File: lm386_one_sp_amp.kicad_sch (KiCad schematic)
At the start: 20 parts, among them J1 AudioJack3, J2 AudioJack2, SW1 SW_SPST, U1 LM386

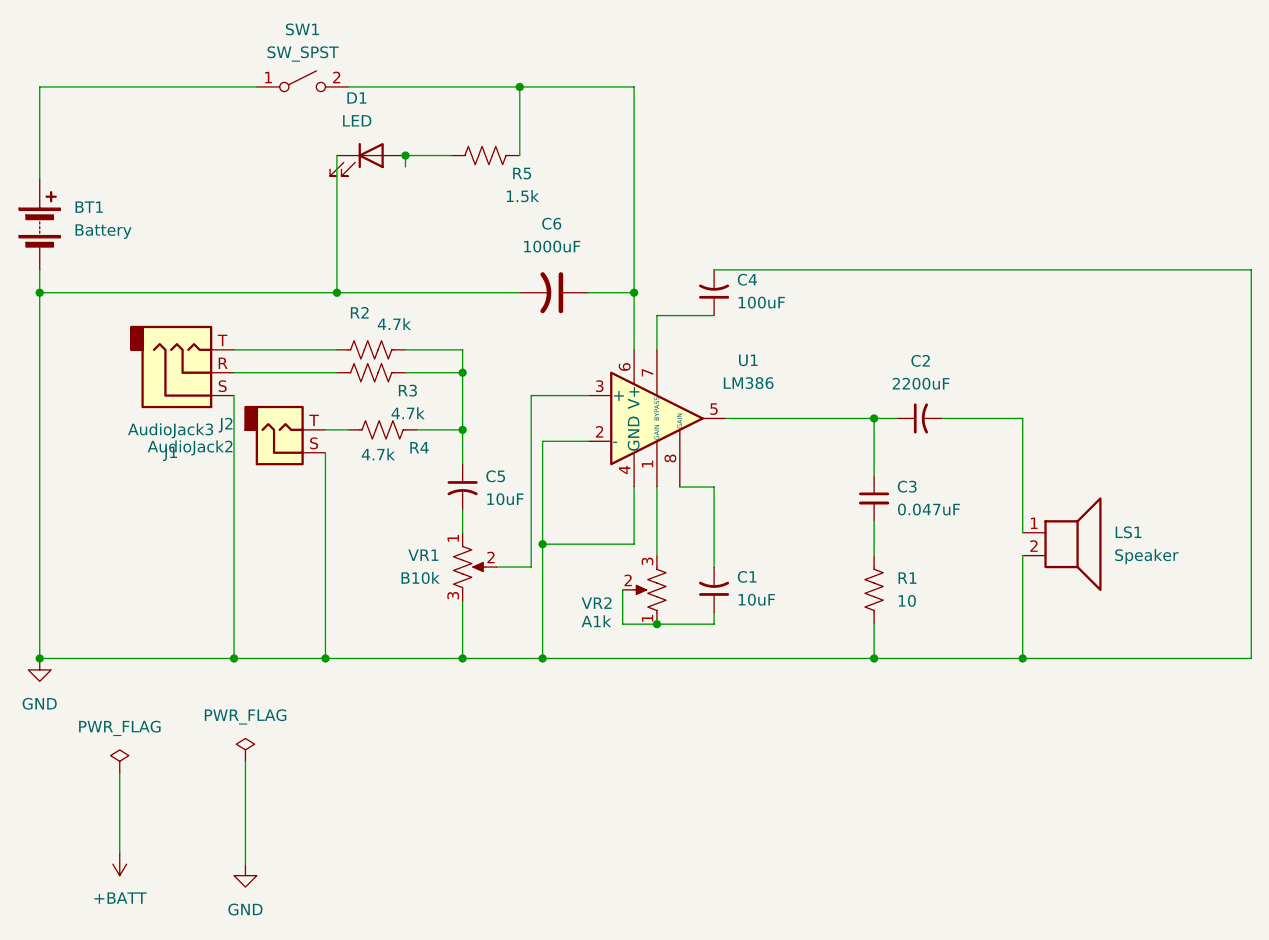
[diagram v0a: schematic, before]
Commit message: ギター接続向けに回路を変更
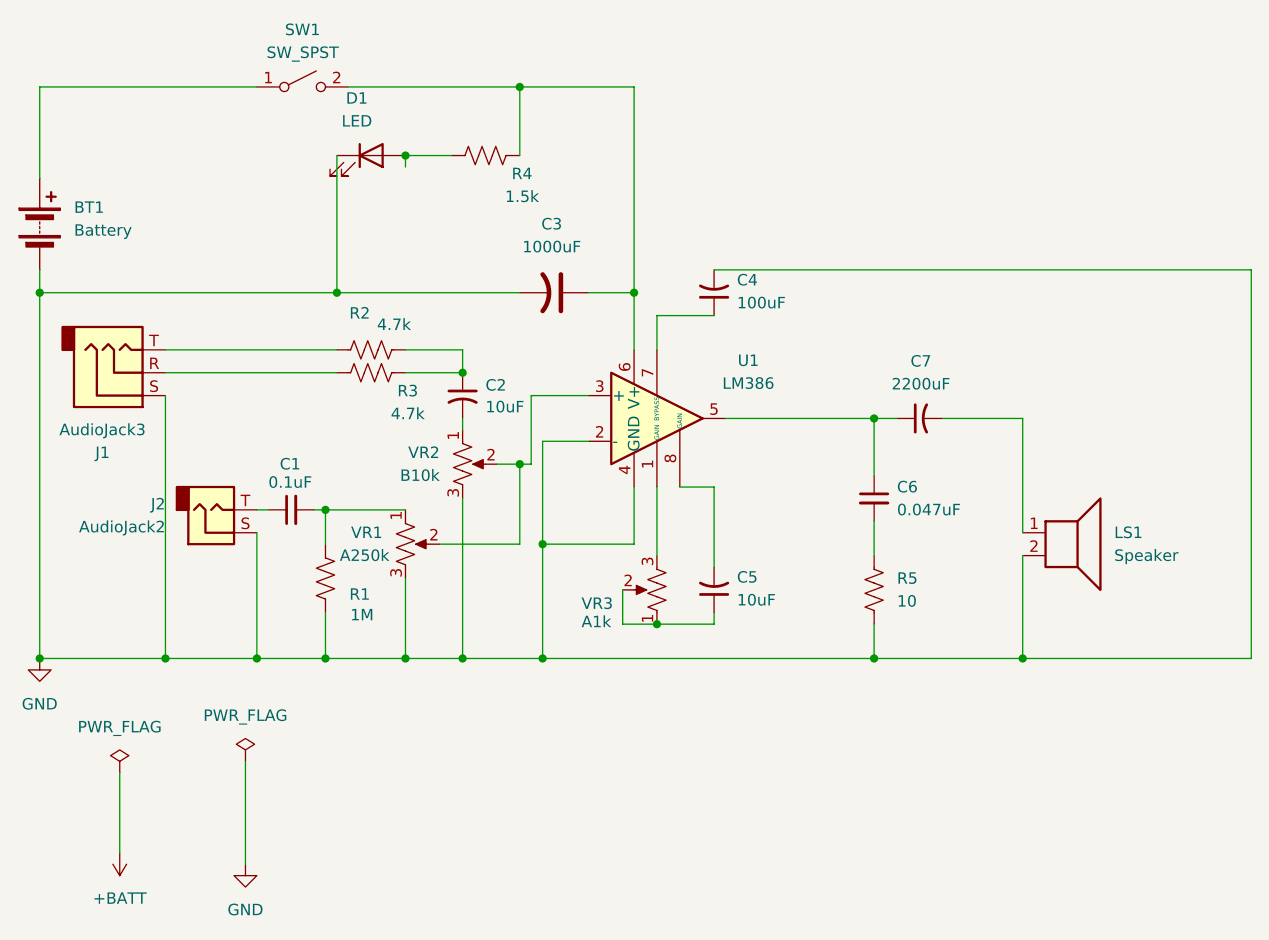
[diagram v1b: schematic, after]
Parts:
- removed R4: 4.7k, Resistor_THT:R_Axial_DIN0204_L3.6mm_D1.6mm_P7.62mm_Horizontal, symbol Device:R_US
- added C1: 0.1uF, Capacitor_THT:C_Disc_D7.0mm_W2.5mm_P5.00mm, symbol Device:C_Small
- added R1: 1M, Resistor_THT:R_Axial_DIN0204_L3.6mm_D1.6mm_P7.62mm_Horizontal, symbol Device:R_US
- added VR1: A250k, symbol Device:R_Potentiometer_US
- renumbered C5 to C2, C6 to C3, C1 to C5, C3 to C6, C2 to C7, R5 to R4, R1 to R5, VR1 to VR2, VR2 to VR3
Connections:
- net GND: now also R1.1, VR1.3
- net at U1.3 (+), VR2.2: now also VR1.2
- net at J2.T: now also C1.1
- new net: C1.2, R1.2, VR1.1
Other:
- moved on the sheet: C2, J1, J2, VR2

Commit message: 基板を作り直す
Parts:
- added R4, R5: 4.7k, Resistor_THT:R_Axial_DIN0204_L3.6mm_D1.6mm_P7.62mm_Horizontal, symbol Device:R_US
- C1: footprint Capacitor_THT:C_Disc_D7.0mm_W2.5mm_P5.00mm -> Capacitor_THT:C_Rect_L10.3mm_W5.0mm_P7.50mm_MKS4
- C6: footprint Capacitor_THT:C_Disc_D7.0mm_W2.5mm_P5.00mm -> Capacitor_THT:C_Rect_L9.0mm_W4.0mm_P7.50mm_MKT
- renumbered R2 to R1, R3 to R2, R1 to R3, R4 to R6, R5 to R7, VR2 to VR1, VR1 to VR2
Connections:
- new net: R4.1, R5.1, U1.3 (+)
- new net: R4.2, VR1.2
- new net: R5.2, VR2.2
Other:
- moved on the sheet: C2, R1, R2, VR1, VR2

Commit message: 配置を進める
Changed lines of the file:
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@@
-	)
-	(junction
-		(at 101.6 66.04)
-		(diameter 0)
-		(color 0 0 0 0)
 	)
 	(junction
@@
 		)
 		(stroke
-			(width 0)
-			(type default)
-		)
-	)
-	(wire
-		(pts
-			(xy 101.6 66.04) (xy 101.6 67.31)
-		)
-		(stroke

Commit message: 配置を修正
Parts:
- added H1, H2, H3, H4: MountingHole, MyLibrary:MountingHole_3.2mm_M3, symbol Mechanical:MountingHole
- added J10: ToLED, MyLibrary:PinHeader_1x01_P2.54mm_Vertical, symbol Connector:Conn_01x01_Pin
- added J11: VR1_2, MyLibrary:PinHeader_1x01_P2.54mm_Vertical, symbol Connector:Conn_01x01_Pin
- added J12: VR2_2, MyLibrary:PinHeader_1x01_P2.54mm_Vertical, symbol Connector:Conn_01x01_Pin
- added J13: VR3_1, MyLibrary:PinHeader_1x01_P2.54mm_Vertical, symbol Connector:Conn_01x01_Pin
- added J14: VR3_3, MyLibrary:PinHeader_1x01_P2.54mm_Vertical, symbol Connector:Conn_01x01_Pin
- added J2: IN1, MyLibrary:PinHeader_1x01_P2.54mm_Vertical, symbol Connector:Conn_01x01_Pin
- added J3: IN2, MyLibrary:PinHeader_1x01_P2.54mm_Vertical, symbol Connector:Conn_01x01_Pin
- added J4: ToSW, MyLibrary:PinHeader_1x01_P2.54mm_Vertical, symbol Connector:Conn_01x01_Pin
- added J6: IN3, MyLibrary:PinHeader_1x01_P2.54mm_Vertical, symbol Connector:Conn_01x01_Pin
- added J7: VR2_1, MyLibrary:PinHeader_1x01_P2.54mm_Vertical, symbol Connector:Conn_01x01_Pin
- added J8: VR1_1, MyLibrary:PinHeader_1x01_P2.54mm_Vertical, symbol Connector:Conn_01x01_Pin
- added J9: FromSW, MyLibrary:PinHeader_1x01_P2.54mm_Vertical, symbol Connector:Conn_01x01_Pin
- C1: footprint Capacitor_THT:C_Rect_L10.3mm_W5.0mm_P7.50mm_MKS4 -> MyLibrary:11.6_7.0_p7.5
- C6: footprint Capacitor_THT:C_Rect_L9.0mm_W4.0mm_P7.50mm_MKT -> MyLibrary:9.3_4.3_p7.5
- renumbered J2 to J5
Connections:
- net at R4.2, VR1.2: now also J11.1 (Pin_1)
- net at C1.2, R3.2, VR2.1: now also J7.1 (Pin_1)
- net at BT1.1 (+), SW1.1 (A): now also J4.1 (Pin_1)
- net at C3.1, R6.2, SW1.2 (B)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: now also J9.1 (Pin_1)
- net at C5.1, VR3.1, VR3.2: now also J13.1 (Pin_1)
- net at U1.1 (GAIN), VR3.3: now also J14.1 (Pin_1)
- net at J1.R, R2.1: now also J3.1 (Pin_1)
- net at J1.T, R1.1: now also J2.1 (Pin_1)
- net at D1.2 (A), R6.1: now also J10.1 (Pin_1)
- net at C2.2, VR1.1: now also J8.1 (Pin_1)
- net at C1.1, J5.T: now also J6.1 (Pin_1)
- net at R5.2, VR2.2: now also J12.1 (Pin_1)
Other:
- moved on the sheet: C5, R1, R2, R4
